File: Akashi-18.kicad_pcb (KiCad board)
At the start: 2 copper layers, 71.1 x 83.8 mm, 12 parts, among them Q1 DTC143Z, Q2 DTC143Z, Q3 DTC143Z, SW1 B3FS, SW2 B3FS, SW3 B3FS, U1 Pico

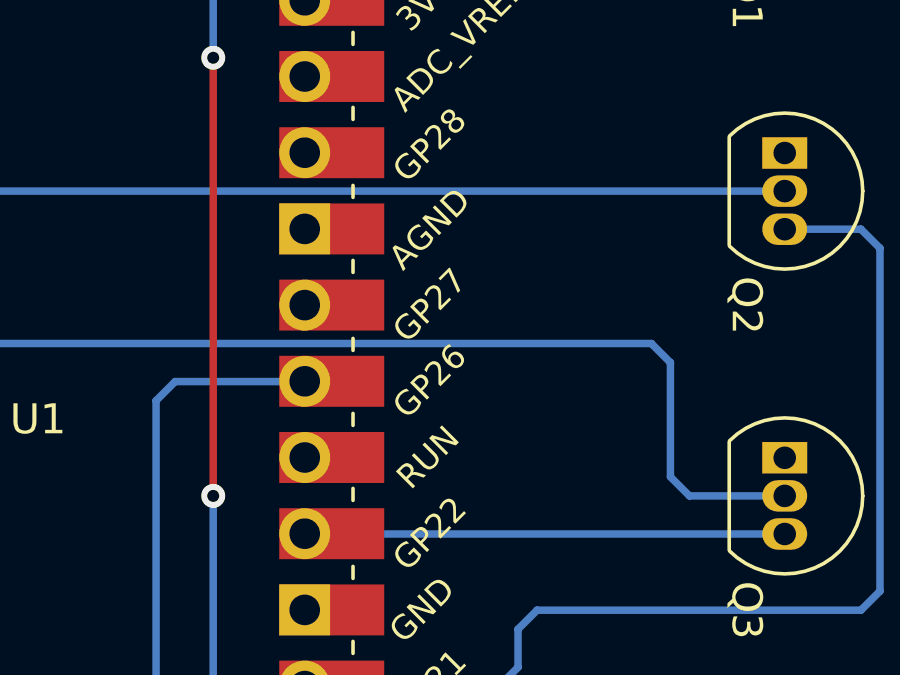
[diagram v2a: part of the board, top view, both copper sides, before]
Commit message: Add capacitor
For RF Immunity reduction.
Also added parts list.
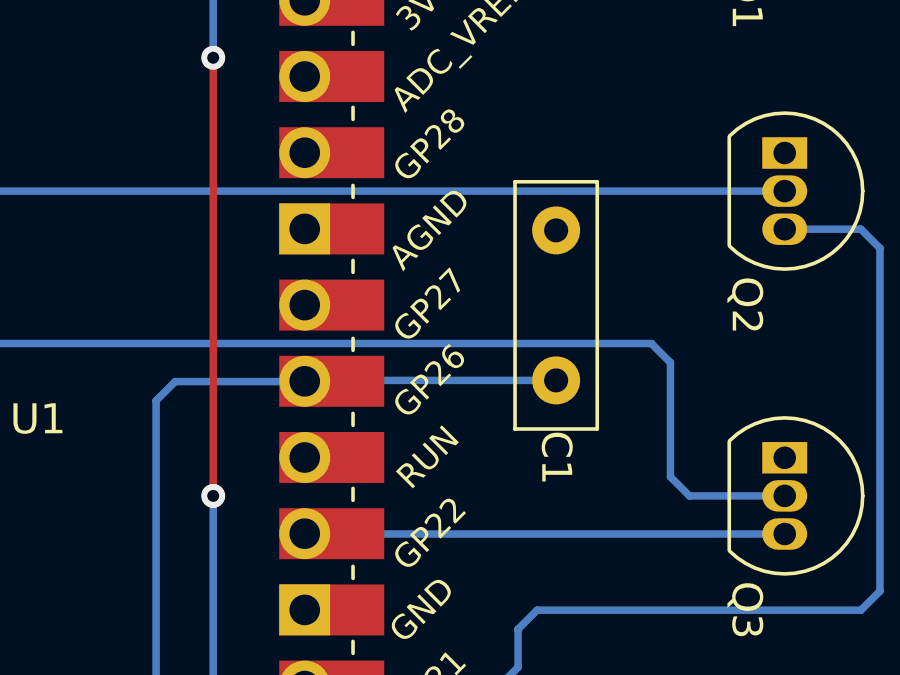
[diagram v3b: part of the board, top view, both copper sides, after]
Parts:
- added C1: C, Capacitor_THT:C_Disc_D8.0mm_W2.5mm_P5.00mm, F.Cu at (141.0, 91.4)
- R1: value 220 -> 150
- R2: value 180 -> 240
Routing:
- net Net-(U1-GPIO26_ADC0): track 36.2 -> 44.6 mm
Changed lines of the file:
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@@
         (effects (font (size 1 1) (thickness 0.15)))
     )
-    (fp_text value "220" (at 5.08 2.37 90) (layer "F.Fab")
+    (fp_text value "150" (at 5.08 2.37 90) (layer "F.Fab")
         (effects (font (size 1 1) (thickness 0.15)))
     )
@@
         (effects (font (size 1 1) (thickness 0.15)))
     )
-    (fp_text value "180" (at 5.08 2.37 90) (layer "F.Fab")
+    (fp_text value "240" (at 5.08 2.37 90) (layer "F.Fab")
         (effects (font (size 1 1) (thickness 0.15)))
     )
@@
       (net 11 "/BLUE") (pinfunction "B") (pintype "input"))
     (model "${KICAD6_3DMODEL_DIR}/Package_TO_SOT_THT.3dshapes/TO-92_Inline.wrl"
+      (offset (xyz 0 0 0))
+      (scale (xyz 1 1 1))
+      (rotate (xyz 0 0 0))
+    )
+  )
+  (footprint "Capacitor_THT:C_Disc_D8.0mm_W2.5mm_P5.00mm" (layer "F.Cu")
+    (at 140.97 91.4 90)
+    (descr "C, Disc series, Radial, pin pitch=5.00mm, , diameter*width=8*2.5mm^2, Capacitor, http://cdn-reichelt.de/documents/datenblatt/B300/DS_KERKO_TC.pdf")
+    (tags "C Disc series Radial pin pitch 5.00mm  diameter 8mm width 2.5mm Capacitor")
+    (property "Sheetfile" "Akashi-18.kicad_sch")
+    (property "Sheetname" "")
+    (property "ki_description" "Unpolarized capacitor")
+    (property "ki_keywords" "cap capacitor")
+    (attr through_hole)
+    (fp_text reference "C1" (at -2.58 0 270 unlocked) (layer "F.SilkS")
+        (effects (font (size 1 1) (thickness 0.15)))
+    )
+    (fp_text value "C" (at 2.5 2.5 90) (layer "F.Fab")
+        (effects (font (size 1 1) (thickness 0.15)))
+    )
+    (fp_text user "${REFERENCE}" (at 2.5 0 90) (layer "F.Fab")
+        (effects (font (size 1 1) (thickness 0.15)))
+    )
+    (fp_line (start -1.62 -1.37) (end -1.62 1.37)
+      (stroke (width 0.12) (type solid)) (layer "F.SilkS"))
+    (fp_line (start -1.62 -1.37) (end 6.62 -1.37)
+      (stroke (width 0.12) (type solid)) (layer "F.SilkS"))
+    (fp_line (start -1.62 1.37) (end 6.62 1.37)
+      (stroke (width 0.12) (type solid)) (layer "F.SilkS"))
+    (fp_line (start 6.62 -1.37) (end 6.62 1.37)
+      (stroke (width 0.12) (type solid)) (layer "F.SilkS"))
+    (fp_line (start -1.75 -1.5) (end -1.75 1.5)
+      (stroke (width 0.05) (type solid)) (layer "F.CrtYd"))
+    (fp_line (start -1.75 1.5) (end 6.75 1.5)
+      (stroke (width 0.05) (type solid)) (layer "F.CrtYd"))
+    (fp_line (start 6.75 -1.5) (end -1.75 -1.5)
+      (stroke (width 0.05) (type solid)) (layer "F.CrtYd"))
+    (fp_line (start 6.75 1.5) (end 6.75 -1.5)
+      (stroke (width 0.05) (type solid)) (layer "F.CrtYd"))
+    (fp_line (start -1.5 -1.25) (end -1.5 1.25)
+      (stroke (width 0.1) (type solid)) (layer "F.Fab"))
+    (fp_line (start -1.5 1.25) (end 6.5 1.25)
+      (stroke (width 0.1) (type solid)) (layer "F.Fab"))
+    (fp_line (start 6.5 -1.25) (end -1.5 -1.25)
+      (stroke (width 0.1) (type solid)) (layer "F.Fab"))
+    (fp_line (start 6.5 1.25) (end 6.5 -1.25)
+      (stroke (width 0.1) (type solid)) (layer "F.Fab"))
+    (pad "1" thru_hole circle (at 0 0 90) (size 1.6 1.6) (drill 0.8) (layers "*.Cu" "*.Mask")
+      (net 12 "Net-(U1-GPIO26_ADC0)") (pintype "passive"))
+    (pad "2" thru_hole circle (at 5 0 90) (size 1.6 1.6) (drill 0.8) (layers "*.Cu" "*.Mask")
+      (net 5 "GND") (pintype "passive"))
+    (model "${KICAD6_3DMODEL_DIR}/Capacitor_THT.3dshapes/C_Disc_D8.0mm_W2.5mm_P5.00mm.wrl"
       (offset (xyz 0 0 0))
       (scale (xyz 1 1 1))
@@
   (segment (start 94.615 87.63) (end 107.95 87.63) (width 0.25) (layer "B.Cu") (net 10))
   (segment (start 132.575 96.52) (end 148.59 96.52) (width 0.25) (layer "B.Cu") (net 11))
+  (segment (start 140.97 91.4) (end 132.62 91.4) (width 0.25) (layer "B.Cu") (net 12))
   (segment (start 140.38 108.63) (end 139.7 107.95) (width 0.25) (layer "B.Cu") (net 12))
   (segment (start 128.27 91.44) (end 132.575 91.44) (width 0.25) (layer "B.Cu") (net 12))
+  (segment (start 132.62 91.4) (end 132.59 91.43) (width 0.25) (layer "B.Cu") (net 12))
   (segment (start 142.86 108.63) (end 140.38 108.63) (width 0.25) (layer "B.Cu") (net 12))
   (segment (start 139.7 107.95) (end 128.27 107.95) (width 0.25) (layer "B.Cu") (net 12))

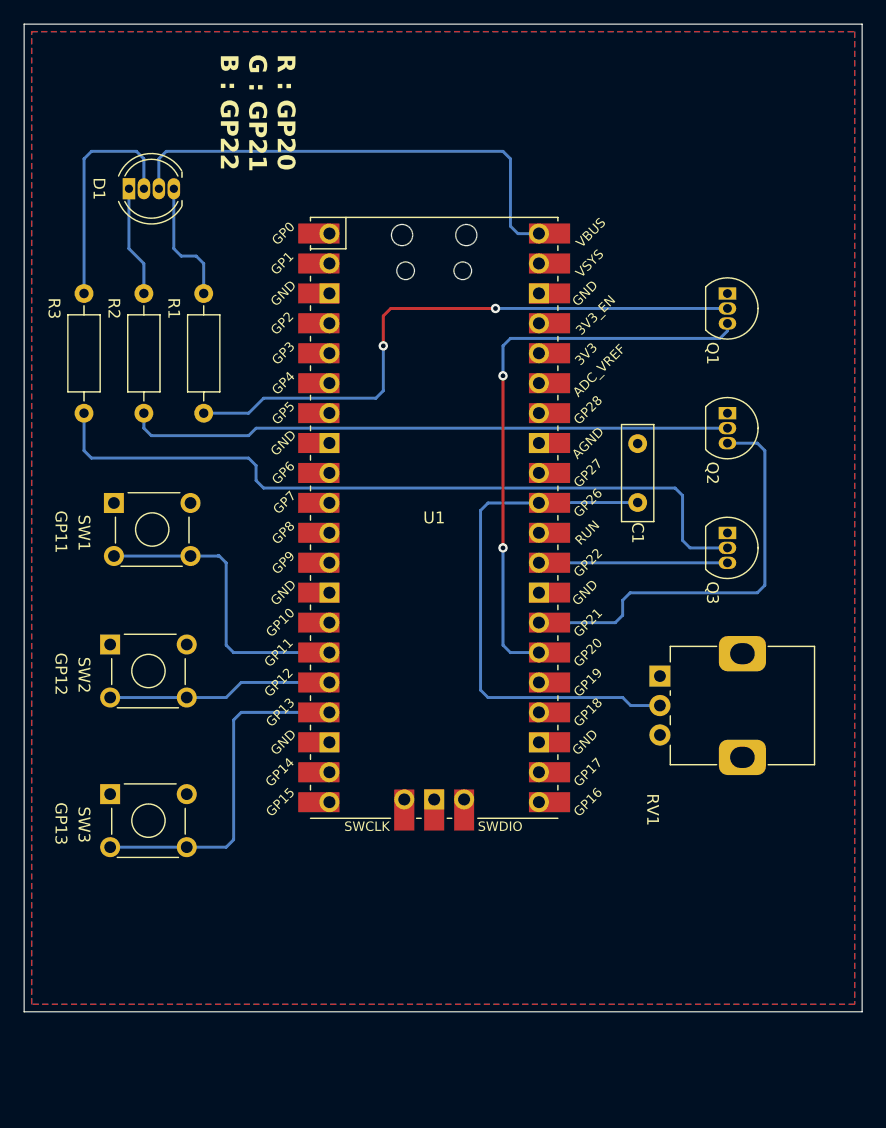
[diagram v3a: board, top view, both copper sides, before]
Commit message: Reshaped to the business card size.
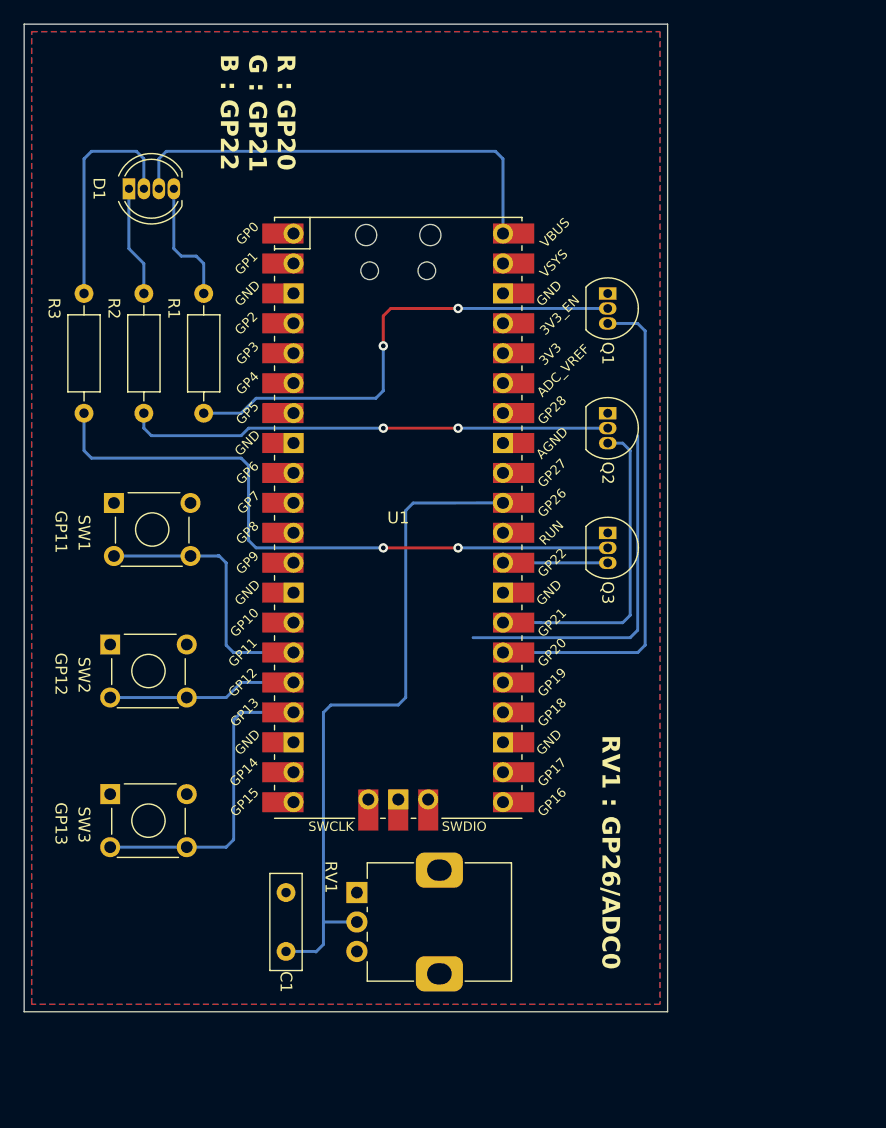
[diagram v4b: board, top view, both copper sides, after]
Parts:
- moved C1 48.4 mm to (111.1, 129.5)
- moved RV1 31.6 mm to (117.1, 124.5)
- moved Q1 10.2 mm to (138.4, 73.7)
- moved Q2 10.2 mm to (138.4, 83.8)
- moved Q3 10.2 mm to (138.4, 94.0)
- moved U1 3.05 mm to (120.7, 92.7)
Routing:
- net /3V3: track 0.00 -> 30.7 mm
- net Net-(U1-GPIO26_ADC0): track 44.6 -> 57.9 mm
- net Net-(Q1-C): track 52.0 -> 41.7 mm
- net Net-(Q2-C): track 51.3 -> 41.2 mm, vias 0 -> 2
- net Net-(Q3-C): track 64.2 -> 54.8 mm, vias 0 -> 2
- net /GREEN: track 36.1 -> 27.2 mm
- net /BLUE: track 16.0 -> 8.89 mm
- net /RED: track 48.9 -> 42.7 mm, vias 2 -> 0
- net Net-(U1-GPIO13): track 29.3 -> 26.3 mm
- net Net-(U1-GPIO12): track 19.1 -> 16.1 mm
- net Net-(U1-GPIO11): track 25.8 -> 22.8 mm
- net +5V: track 41.3 -> 38.6 mm
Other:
- board size 71.1 x 83.8 mm -> 54.6 x 83.8 mm
- board text added: "RV1 : GP26/ADC0"

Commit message: Refine the size and placement.
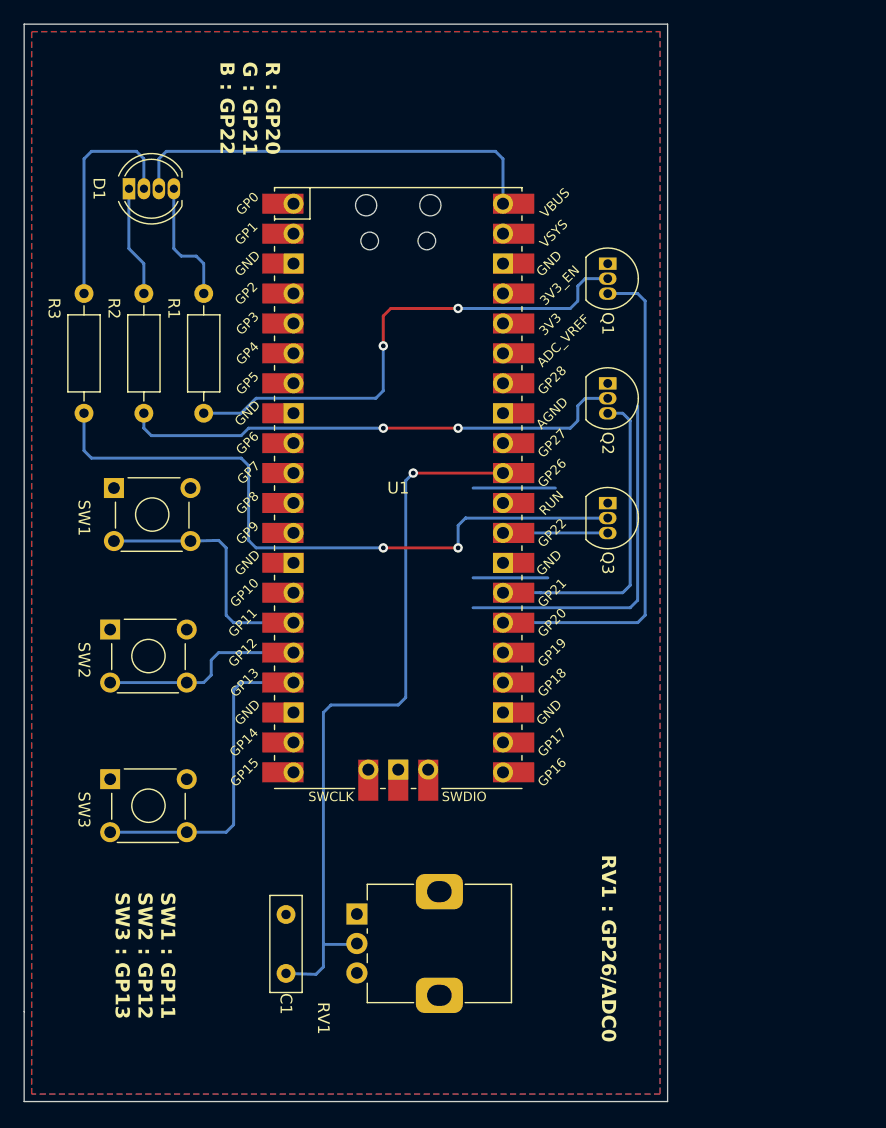
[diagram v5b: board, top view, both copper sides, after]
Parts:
- C1: value C -> 0.1u
- moved Q1 2.53 mm to (138.4, 71.1)
- moved Q3 2.53 mm to (138.4, 91.5)
- moved U1 2.53 mm to (120.7, 90.2)
- moved Q2 2.53 mm to (138.4, 81.3)
- moved C1 1.87 mm to (111.1, 131.4)
- moved RV1 1.83 mm to (117.1, 126.3)
- moved SW3 1.27 mm to (96.2, 114.9)
- moved SW1 1.27 mm to (96.5, 90.2)
- moved SW2 1.27 mm to (96.2, 102.2)
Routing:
- net /3V3: track 30.7 -> 44.1 mm
- net Net-(U1-GPIO26_ADC0): track 57.9 -> 62.3 mm, vias 0 -> 1
- net +5V: track 38.6 -> 36.1 mm
- net Net-(Q3-C): track 54.8 -> 56.9 mm
- net Net-(Q1-C): track 41.7 -> 43.5 mm
- net Net-(Q2-C): track 41.2 -> 43.0 mm
- net Net-(U1-GPIO11): track 22.8 -> 21.5 mm
- net Net-(U1-GPIO12): track 16.1 -> 17.4 mm
- net Net-(U1-GPIO13): track 26.3 -> 27.5 mm
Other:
- board size 54.6 x 83.8 mm -> 54.6 x 91.4 mm
- board text added: "SW1 : GP11 SW2 : GP12 SW3 : GP13"
- board text removed: "GP11"
- board text removed: "GP12"
- board text removed: "GP13"
